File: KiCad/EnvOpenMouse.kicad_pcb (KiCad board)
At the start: 2 copper layers, 184 x 176.6 mm, 59 parts, among them J2 Conn_01x03, J3 Conn_01x03, J4 Conn_01x03, J5 Conn_01x03, J8 TSA343G00-250J2, J9 C145960, SW1 SW_Push_SPDT, SW2 SW_Push_SPDT, SW3 SW_Push_SPDT, U1 TLV70218DBVR, U2 PMW3360DM-T2QU, U3 SOT-23-5 5.5V 3.3V 500mA, U4 RP2040, Y1 3225_4P

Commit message: I dont even remember what I changed.
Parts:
- removed J4: Conn_01x03, Connector_PinHeader_2.54mm:PinHeader_1x03_P2.54mm_Vertical
- moved VR1 104.2 mm to (38.0, 44.2)
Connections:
- U4 pad 2: /RP2040/GPIO0 -> ROT-B
- U4 pad 3: /RP2040/GPIO1 -> ROT-A
- VR1 pad A: Net-(J4-Pad3) -> ROT-A
- VR1 pad B: Net-(J4-Pad2) -> GND
- VR1 pad C: Net-(J4-Pad1) -> ROT-B
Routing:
- net ROT-A: track 0.00 -> 19.7 mm
- net Net-(J4-Pad3): track 18.4 -> 0.00 mm
- net Net-(J4-Pad2): track 15.1 -> 0.00 mm
- net ROT-B: track 0.00 -> 12.6 mm
- net Net-(J4-Pad1): track 11.3 -> 0.00 mm

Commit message: decided to work on this again | made PCB have reasonableish dimensions and moved mouse buttons to suitable positions
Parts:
- removed H1, H2, H3, H4: MountingHole_Pad, MountingHole:MountingHole_2.2mm_M2
- removed J2, J3, J5: Conn_01x03, Connector_PinHeader_2.54mm:PinHeader_1x03_P2.54mm_Vertical
- added C16: 100nf 0402, Capacitor_SMD:C_0402_1005Metric, F.Cu at (48.8, 78.7)
- added C20: 10uf 0402, Capacitor_SMD:C_0402_1005Metric, F.Cu at (48.8, 77.7)
- moved SW1 126.6 mm to (32.3, 32.6)
- moved SW3 125.6 mm to (54.3, 32.6)
- moved SW2 119.1 mm to (50.9, 50.7)
- moved J8 27.6 mm to (40.4, 70.9)
- moved C18 27.0 mm to (45.6, 77.3)
- moved C5 27.0 mm to (48.2, 71.9)
- moved R15 27.0 mm to (42.9, 89.9)
- moved U3 27.0 mm to (45.9, 72.6)
- moved U4 27.0 mm to (43.7, 82.6)
- moved C1 27.0 mm to (36.8, 99.2)
- moved C10 27.0 mm to (49.5, 83.6)
- moved C12 27.0 mm to (38.1, 83.6)
- moved C15 27.0 mm to (44.1, 77.5)
- moved C17 27.0 mm to (46.6, 77.3)
- moved C19 27.0 mm to (41.2, 74.1)
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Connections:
- SW1 pad 1: Net-(J2-Pad1) -> MB-1-A
- SW1 pad 2: Net-(J2-Pad2) -> MB-1-B
- SW1 pad 3: Net-(J2-Pad3) -> unconnected-(SW1-Pad3)
- SW2 pad 1: Net-(J3-Pad1) -> MB-2-A
- SW2 pad 2: Net-(J3-Pad2) -> MB-2-B
- SW2 pad 3: Net-(J3-Pad3) -> unconnected-(SW2-Pad3)
- SW3 pad 1: Net-(J5-Pad1) -> MB-3-A
- SW3 pad 2: Net-(J5-Pad2) -> MB-3-B
- SW3 pad 3: Net-(J5-Pad3) -> unconnected-(SW3-Pad3)
- U4 pad 4: /RP2040/GPIO2 -> MB-1-A
- U4 pad 5: /RP2040/GPIO3 -> MB-1-B
- U4 pad 6: /RP2040/GPIO4 -> MB-2-A
- U4 pad 7: /RP2040/GPIO5 -> MB-2-B
- U4 pad 8: /RP2040/GPIO6 -> MB-3-A
- U4 pad 9: /RP2040/GPIO7 -> MB-3-B
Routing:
- net VBUS: track 55.3 -> 15.5 mm, vias 3 -> 2
- net ROT-A: track 19.7 -> 0.00 mm
- net Net-(J5-Pad2): track 16.8 -> 0.00 mm
- net Net-(J3-Pad2): track 16.8 -> 0.00 mm
- net Net-(J2-Pad2): track 16.4 -> 0.00 mm
- net USB_D-: track 13.9 -> 0.00 mm
- net USB_D+: track 13.8 -> 0.00 mm
- net GND: track 0.58 -> 14.0 mm, vias 8 -> 7
- net ROT-B: track 12.6 -> 0.00 mm
- net Net-(J2-Pad3): track 9.50 -> 0.00 mm
- net Net-(J5-Pad3): track 9.43 -> 0.00 mm
- net Net-(J3-Pad3): track 9.43 -> 0.00 mm
- net Net-(J2-Pad1): track 4.43 -> 0.00 mm
- net Net-(J5-Pad1): track 4.34 -> 0.00 mm
- net Net-(J3-Pad1): track 4.34 -> 0.00 mm
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- added copper zone on F.Cu, net +3V3
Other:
- board size 184 x 176.6 mm -> 40 x 110 mm
- board text removed: "A/B/C"
- board text removed: "GND 5V 3.3V MOT/GP1 SCLK/GP2 MOSI/GP3 MISO/GP4 NCS/GP9"

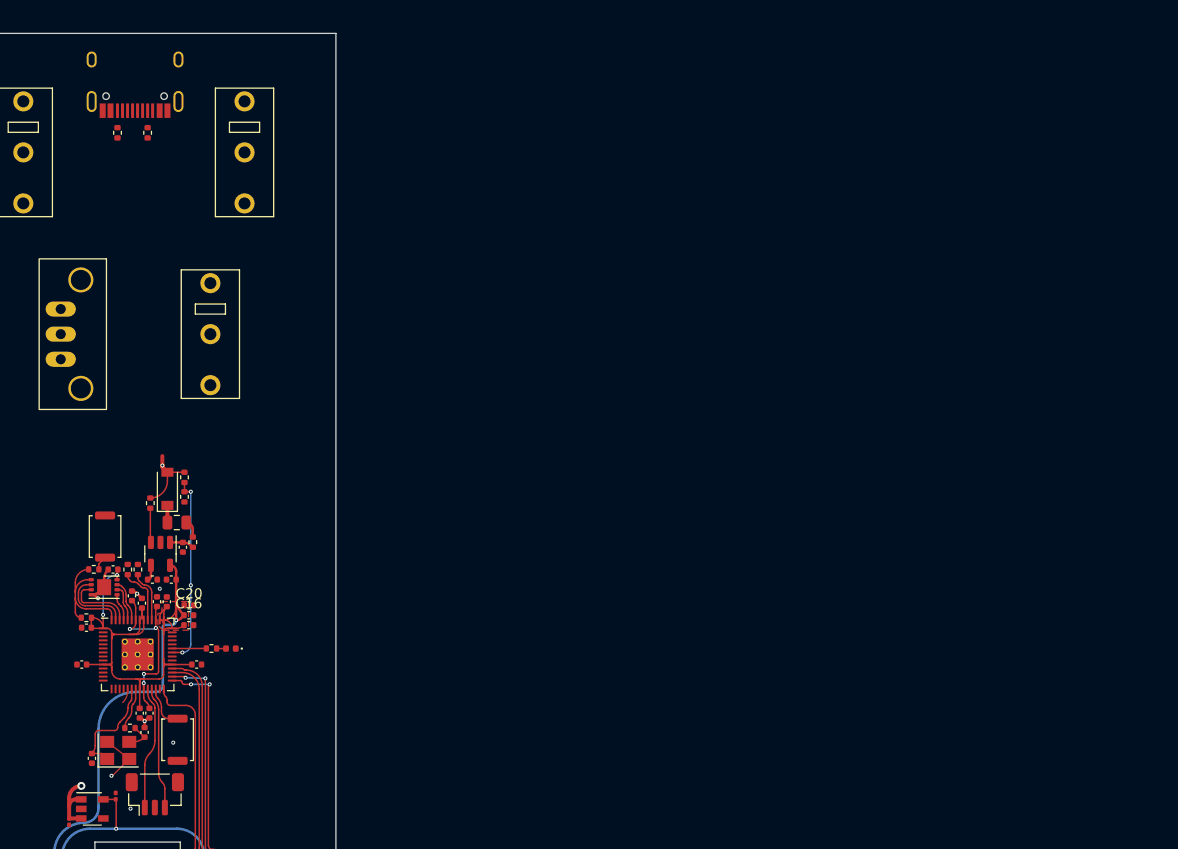
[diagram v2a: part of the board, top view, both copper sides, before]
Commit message: routed some more traces
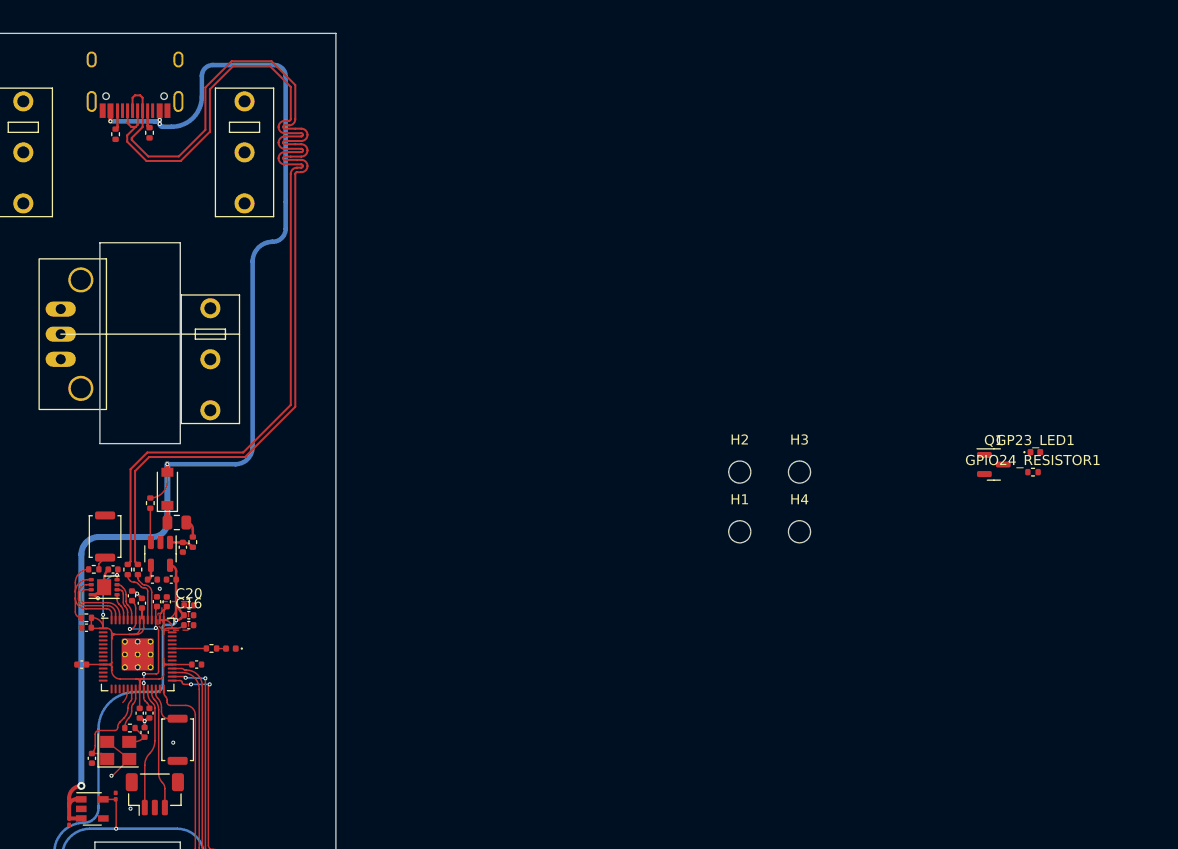
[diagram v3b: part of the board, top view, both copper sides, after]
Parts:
- removed R10: 10K 0402, Resistor_SMD:R_0402_1005Metric
- removed R5: 5.6K 0402, Resistor_SMD:R_0402_1005Metric
- added GP23_LED1: GP23 LED_0402, LED_SMD:LED_0402_1005Metric, F.Cu at (133.1, 62.5)
- added GPIO24_RESISTOR1: 1K 0402, Resistor_SMD:R_0402_1005Metric, F.Cu at (132.8, 64.4)
- added H1: MountingHole_Pad, MountingHole:MountingHole_2.2mm_M2, F.Cu at (103.6, 70.4)
- added H2: MountingHole_Pad, MountingHole:MountingHole_2.2mm_M2, F.Cu at (103.6, 64.4)
- added H3: MountingHole_Pad, MountingHole:MountingHole_2.2mm_M2, F.Cu at (109.6, 64.4)
- added H4: MountingHole_Pad, MountingHole:MountingHole_2.2mm_M2, F.Cu at (109.6, 70.4)
- added Q1: SI2301B, Package_TO_SOT_SMD:SOT-23, F.Cu at (128.9, 63.7)
- moved SW2 2.50 mm to (50.9, 53.2)
- moved R7 0.24 mm to (41.5, 30.8)
- moved R3 0.19 mm to (44.8, 30.6)
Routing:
- net VBUS: track 15.5 -> 123.7 mm, vias 2 -> 5
- net USB_D-: track 0.00 -> 103.6 mm
- net USB_D+: track 0.00 -> 102.0 mm
- net /RP2040/GPIO24: track 19.0 -> 0.00 mm, vias 3 -> 0
- net Net-(R7-Pad2): track 0.00 -> 1.91 mm
- net Net-(R3-Pad2): track 0.00 -> 1.77 mm
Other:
- outline, holes or cut-outs redrawn

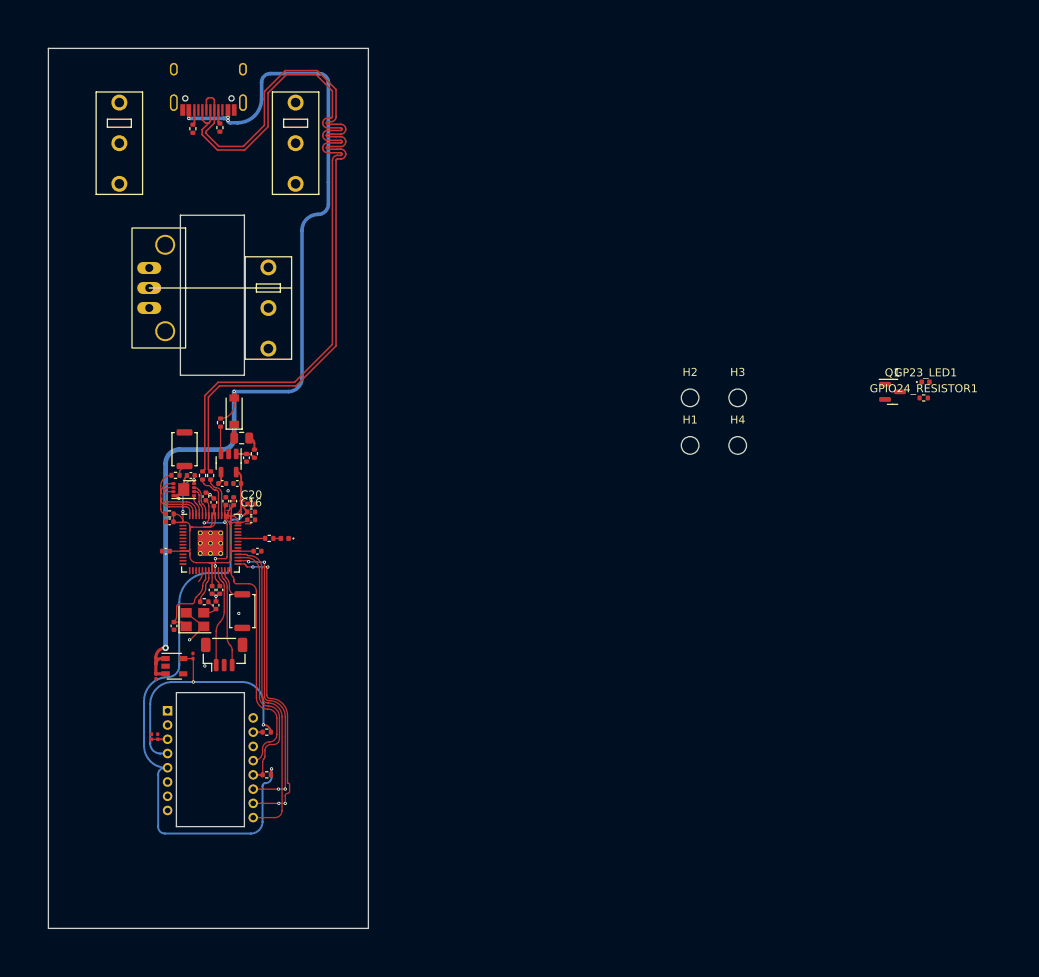
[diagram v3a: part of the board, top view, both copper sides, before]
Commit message: ran traces for parts previously left disconnected and moved about some to improve ease of routing and also shortened PCB down to 94mm along with slimmed width + mount holes
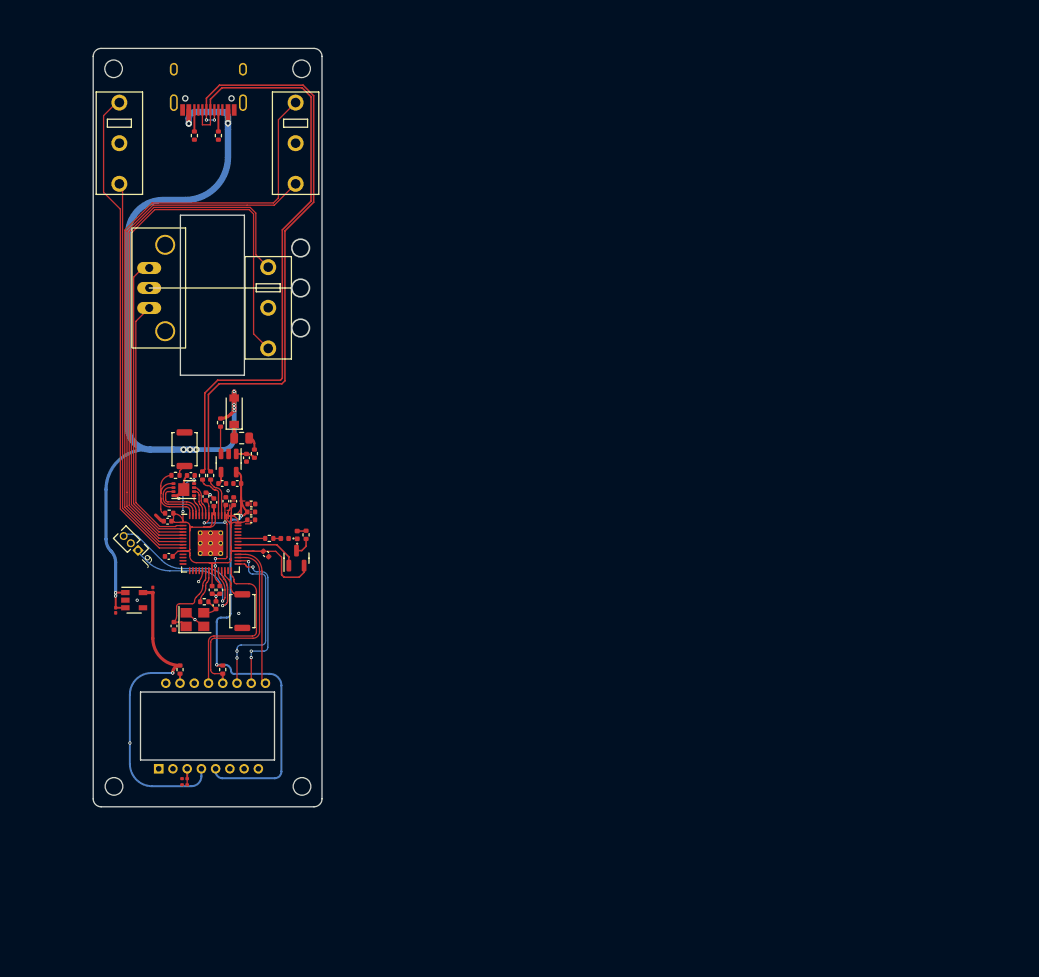
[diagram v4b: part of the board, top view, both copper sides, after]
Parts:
- J9: footprint Connector_JST:JST_SH_BM03B-SRSS-TB_1x03-1MP_P1.00mm_Vertical -> Connector_PinHeader_1.27mm:PinHeader_1x03_P1.27mm_Vertical
- moved H4 88.9 mm to (31.6, 113.0)
- moved H1 86.1 mm to (31.6, 23.3)
- moved GP23_LED1 80.8 mm to (54.5, 81.6), turned to 90 degrees
- moved GPIO24_RESISTOR1 79.1 mm to (55.6, 81.6), turned to -90 degrees
- moved Q1 77.3 mm to (54.4, 84.5), turned to 90 degrees
- moved H3 73.0 mm to (55.1, 113.0)
- moved H2 63.6 mm to (55.0, 23.3)
- moved SW1 27.7 mm to (50.9, 53.2)
- moved SW3 22.0 mm to (32.3, 32.6)
- moved SW2 20.9 mm to (54.3, 32.6)
- moved J9 16.9 mm to (34.6, 83.5), turned to -135 degrees
- moved R2 14.3 mm to (45.2, 98.4), turned to -90 degrees
- moved R1 13.4 mm to (39.9, 98.4), turned to -90 degrees
- moved C2 9.66 mm to (36.5, 88.5)
- moved C1 9.66 mm to (31.8, 91.0)
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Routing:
- net MB-2-B: track 0.00 -> 77.4 mm
- net MB-1-A: track 0.00 -> 76.1 mm
- net MB-1-B: track 0.00 -> 67.3 mm
- net MB-2-A: track 0.00 -> 66.6 mm
- net MB-3-B: track 0.00 -> 62.5 mm
- net MB-3-A: track 0.00 -> 50.2 mm
- net ROT-A: track 0.00 -> 38.2 mm
- net ROT-B: track 0.00 -> 32.2 mm
- net USB_D-: track 103.6 -> 76.7 mm, vias 0 -> 2
- net USB_D+: track 102.0 -> 76.7 mm
- net MOTION/GPIO1: track 39.6 -> 18.6 mm
- net SCLK/GPIO2: track 39.4 -> 19.7 mm, vias 4 -> 3
- net MOSI/GPIO3: track 37.1 -> 21.3 mm, vias 4 -> 3
- net /RP2040/SWD: track 12.1 -> 23.6 mm, vias 0 -> 1
- net +1V8: track 33.1 -> 42.4 mm
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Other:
- board size 40 x 110 mm -> 28.6 x 94.8 mm

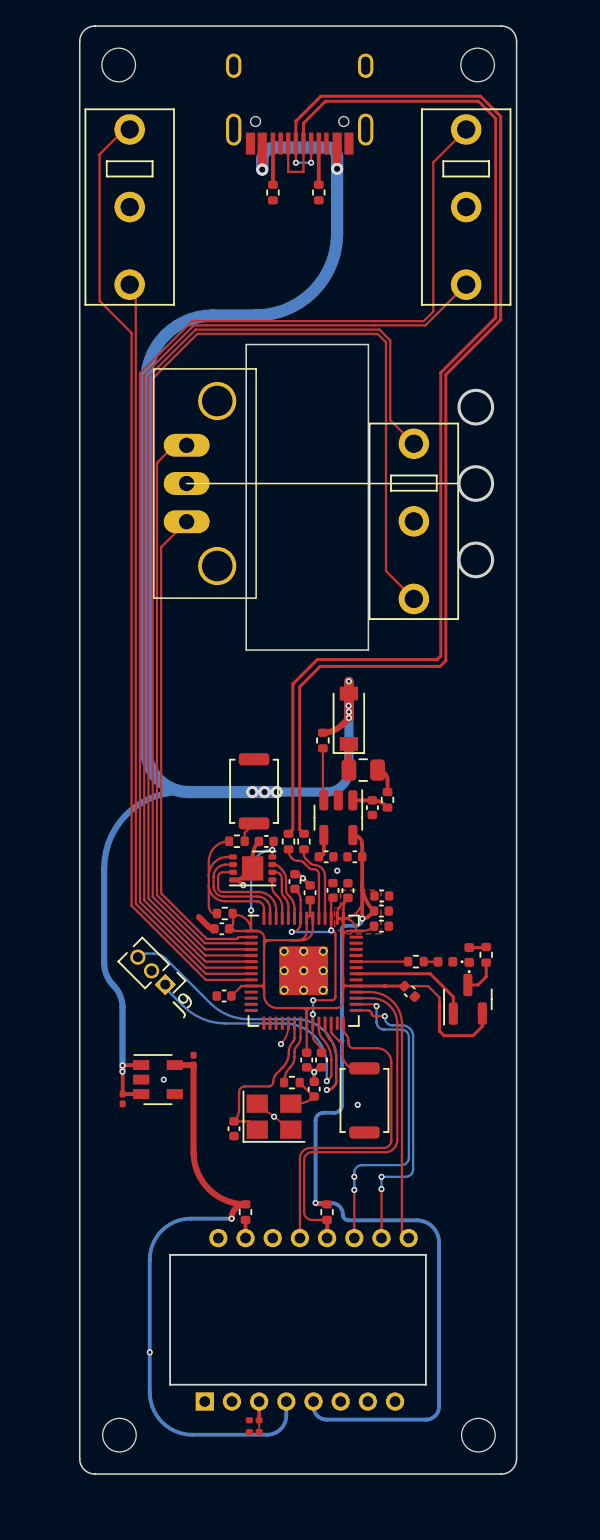
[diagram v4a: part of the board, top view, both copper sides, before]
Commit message: adjusted position of some parts and re-routed related traces, might do that again to compact everything
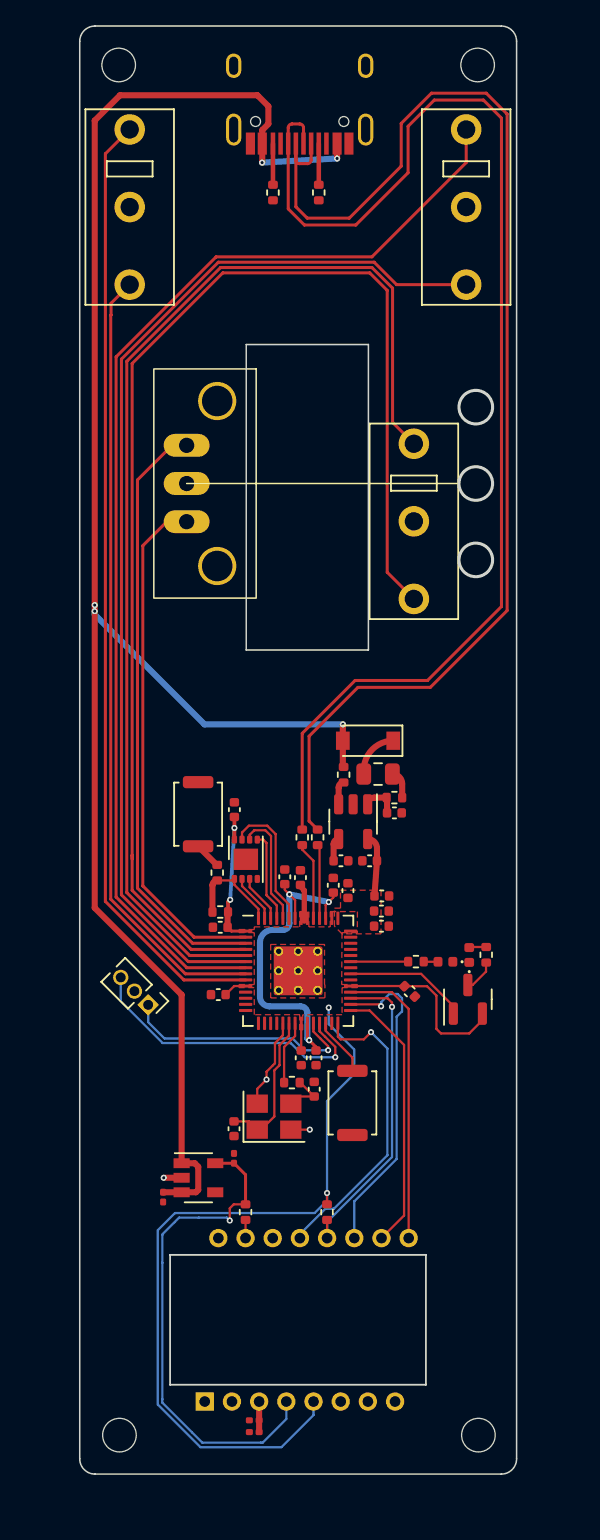
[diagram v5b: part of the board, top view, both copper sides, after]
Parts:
- moved C1 6.95 mm to (34.5, 97.4)
- moved U1 6.95 mm to (36.8, 96.2)
- moved C2 6.95 mm to (39.1, 94.9)
- moved J8 3.96 mm to (36.8, 72.3)
- moved C19 2.94 mm to (39.1, 72.0), turned to 90 degrees
- moved R8 2.62 mm to (46.3, 69.8)
- moved R14 2.43 mm to (38.0, 76.2), turned to 90 degrees
- moved D1 1.91 mm to (47.9, 67.5), turned to 180 degrees
- moved J9 1.74 mm to (33.5, 84.8)
- moved C5 1.48 mm to (49.6, 72.3), turned to 0 degrees
- moved C15 1.17 mm to (43.5, 76.5)
- moved C6 1.00 mm to (48.0, 75.4)
- moved CBP1 1.00 mm to (46.1, 75.4)
- moved F1 1.00 mm to (48.5, 69.7)
- moved U3 1.00 mm to (46.9, 72.8)
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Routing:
- net +3V3: track 135.1 -> 82.4 mm
- net +1V8: track 42.4 -> 33.1 mm, vias 2 -> 1
- net MB-1-B: track 67.3 -> 75.5 mm
- net MB-1-A: track 76.1 -> 84.3 mm
- net /RP2040/QSPI_SS: track 13.1 -> 6.62 mm
- net USB_D-: track 76.7 -> 82.5 mm, vias 2 -> 0
- net VBUS: track 114.3 -> 120.1 mm, vias 11 -> 5
- net USB_D+: track 76.7 -> 82.4 mm
- net +1V1: track 17.7 -> 22.6 mm, vias 4 -> 3
- net /RP2040/QSPI_SD3: track 4.14 -> 8.95 mm
- net GND: track 13.1 -> 8.37 mm, vias 8 -> 3
- net MB-2-A: track 66.6 -> 70.8 mm
- net /RP2040/QSPI_SD1: track 7.39 -> 3.19 mm
- net /RP2040/QSPI_SCLK: track 3.56 -> 7.70 mm
- net /RP2040/SWD: track 23.6 -> 19.8 mm
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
